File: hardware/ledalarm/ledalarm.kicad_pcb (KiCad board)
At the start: 4 copper layers, 32 x 52 mm, 17 parts, among them J1 Conn_01x07_Pin

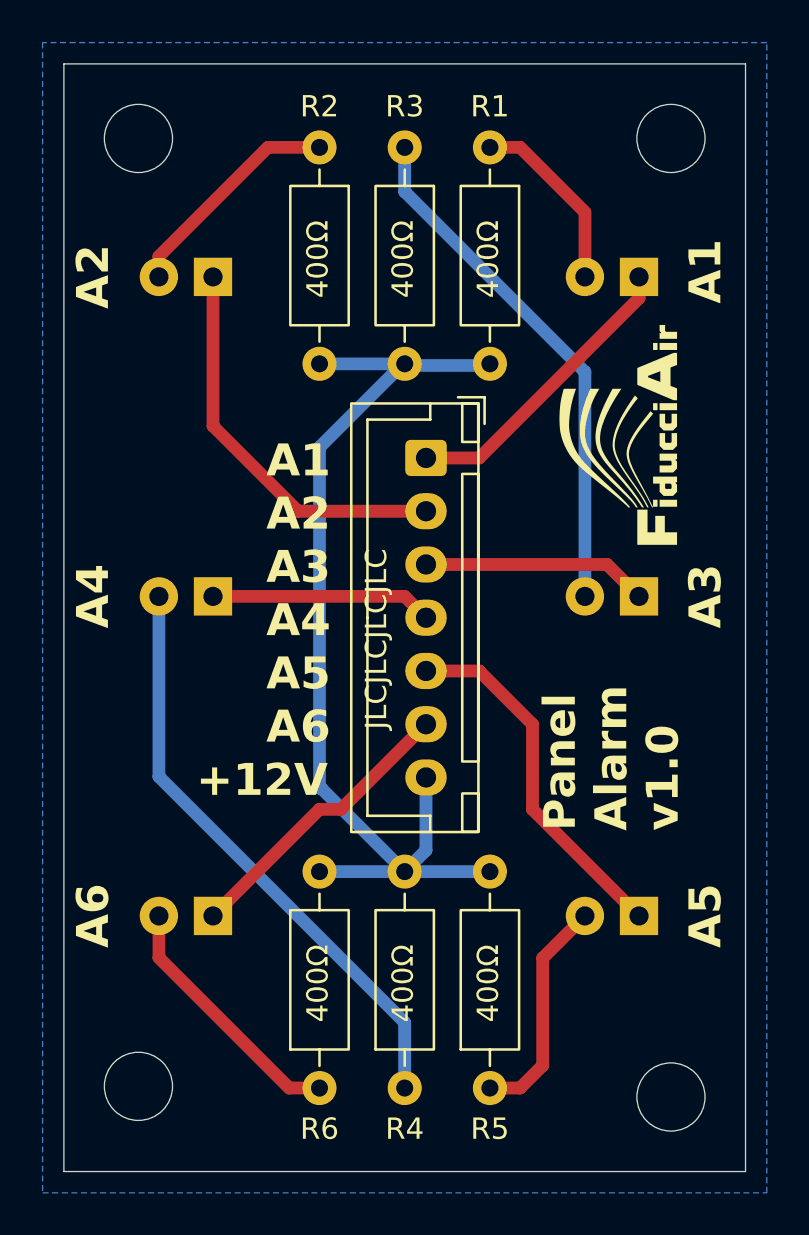
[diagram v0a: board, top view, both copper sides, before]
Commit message: Optional BLE notify, reorg startup
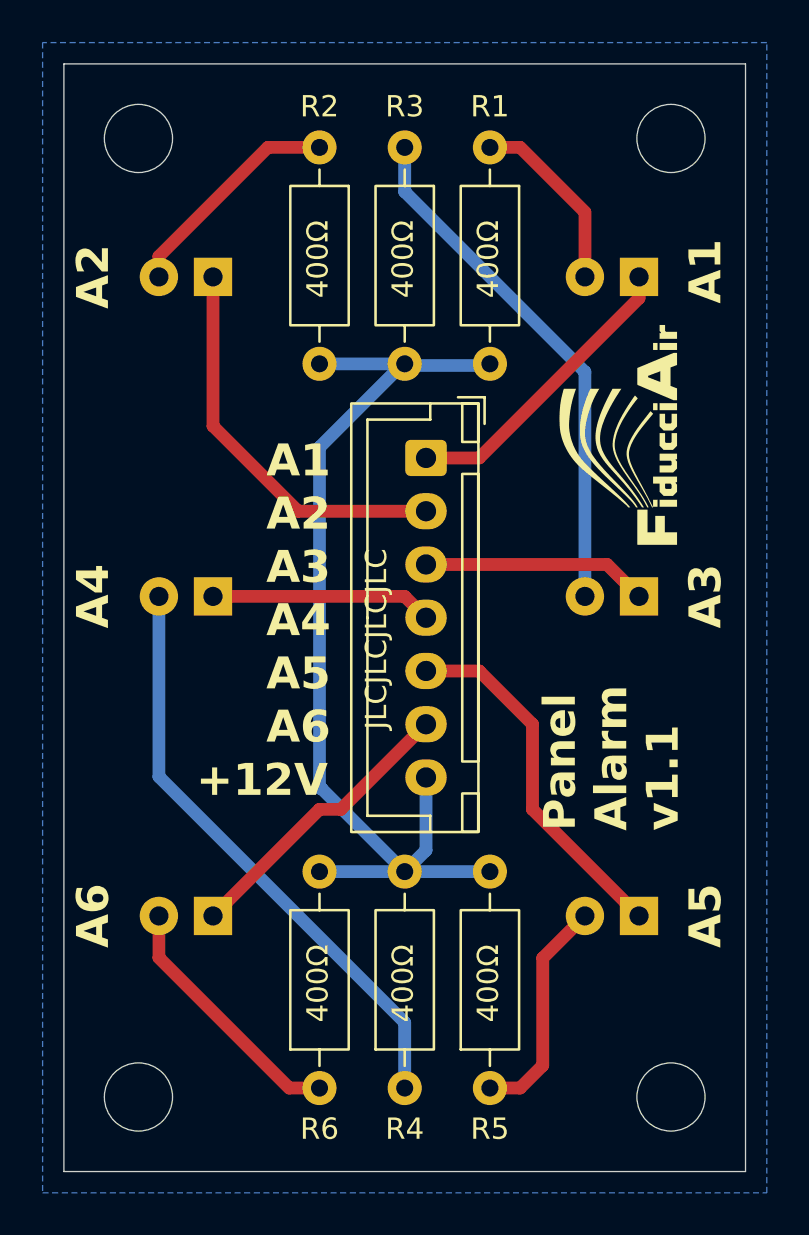
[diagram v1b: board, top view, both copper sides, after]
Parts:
- moved REF** 0.50 mm to (2.50, 48.5)
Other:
- board text added: "Panel Alarm v1.1"
- board text removed: "Panel Alarm v1.0"
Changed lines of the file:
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@@
 	(footprint "MountingHole:MountingHole_3.2mm_M3"
 		(layer "F.Cu")
-		(at 2.5 48)
+		(at 2.5 48.5)
 		(descr "Mounting Hole 3.2mm, M3, no annular, generated by kicad-footprint-generator mountinghole.py")
 		(tags "mountinghole M3")
@@
 		)
 	)
-	(gr_text "Panel\nAlarm\nv1.0"
+	(gr_text "Panel\nAlarm\nv1.1"
 		(at 28 36 90)
 		(layer "F.SilkS")
@@
 	)
 	(segment
-		(start 15 6)
-		(end 23.46 14.46)
-		(width 0.6)
-		(layer "B.Cu")
-		(net "Net-(D3-A)")
-	)
-	(segment
-		(start 23.46 14.46)
-		(end 23.46 25)
-		(width 0.6)
-		(layer "B.Cu")
-		(net "Net-(D3-A)")
-	)
-	(segment
-		(start 15 4)
-		(end 15 6)
-		(width 0.6)
-		(layer "B.Cu")
-		(net "Net-(D3-A)")
-	)
-	(segment
 		(start 3.46 40)
 		(end 3.46 41.96)
@@
 		(net "Net-(D6-A)")
 	)
+	(segment
+		(start 15 6)
+		(end 23.46 14.46)
+		(width 0.6)
+		(layer "B.Cu")
+		(net "Net-(D3-A)")
+	)
+	(segment
+		(start 23.46 14.46)
+		(end 23.46 25)
+		(width 0.6)
+		(layer "B.Cu")
+		(net "Net-(D3-A)")
+	)
+	(segment
+		(start 15 4)
+		(end 15 6)
+		(width 0.6)
+		(layer "B.Cu")
+		(net "Net-(D3-A)")
+	)
 	(zone
